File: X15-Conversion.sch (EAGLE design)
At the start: 28 parts, among them U2 LINEAR,AZ1117CR-3.3TRG1DIODES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

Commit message: added files
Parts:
- R7: value 150 -> 600
- R8: value 150 -> 300
- R9: value 150 -> 200
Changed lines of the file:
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@@
 <part name="CONN1" library="CONN, Distribution-Conversion (3)" deviceset="CONVERSION-DISTRIBUTION" device=""/>
 <part name="D4" library="SparkFun-LED" library_urn="urn:adsk.eagle:library:529" deviceset="LED-YELLOW" device="0603" package3d_urn="urn:adsk.eagle:package:39354/1" value="Yellow"/>
-<part name="R7" library="SparkFun-Resistors" library_urn="urn:adsk.eagle:library:532" deviceset="20OHM" device="-0603-1/10W-1%" package3d_urn="urn:adsk.eagle:package:39650/1" value="150"/>
-<part name="R8" library="SparkFun-Resistors" library_urn="urn:adsk.eagle:library:532" deviceset="20OHM" device="-0603-1/10W-1%" package3d_urn="urn:adsk.eagle:package:39650/1" value="150"/>
-<part name="R9" library="SparkFun-Resistors" library_urn="urn:adsk.eagle:library:532" deviceset="20OHM" device="-0603-1/10W-1%" package3d_urn="urn:adsk.eagle:package:39650/1" value="150"/>
+<part name="R7" library="SparkFun-Resistors" library_urn="urn:adsk.eagle:library:532" deviceset="20OHM" device="-0603-1/10W-1%" package3d_urn="urn:adsk.eagle:package:39650/1" value="600"/>
+<part name="R8" library="SparkFun-Resistors" library_urn="urn:adsk.eagle:library:532" deviceset="20OHM" device="-0603-1/10W-1%" package3d_urn="urn:adsk.eagle:package:39650/1" value="300"/>
+<part name="R9" library="SparkFun-Resistors" library_urn="urn:adsk.eagle:library:532" deviceset="20OHM" device="-0603-1/10W-1%" package3d_urn="urn:adsk.eagle:package:39650/1" value="200"/>
 <part name="FRAME3" library="frames" library_urn="urn:adsk.eagle:library:229" deviceset="A4L-LOC" device=""/>
 <part name="D6" library="SparkFun-LED" library_urn="urn:adsk.eagle:library:529" deviceset="LED-RED" device="0603" package3d_urn="urn:adsk.eagle:package:39354/1" value="RED"/>

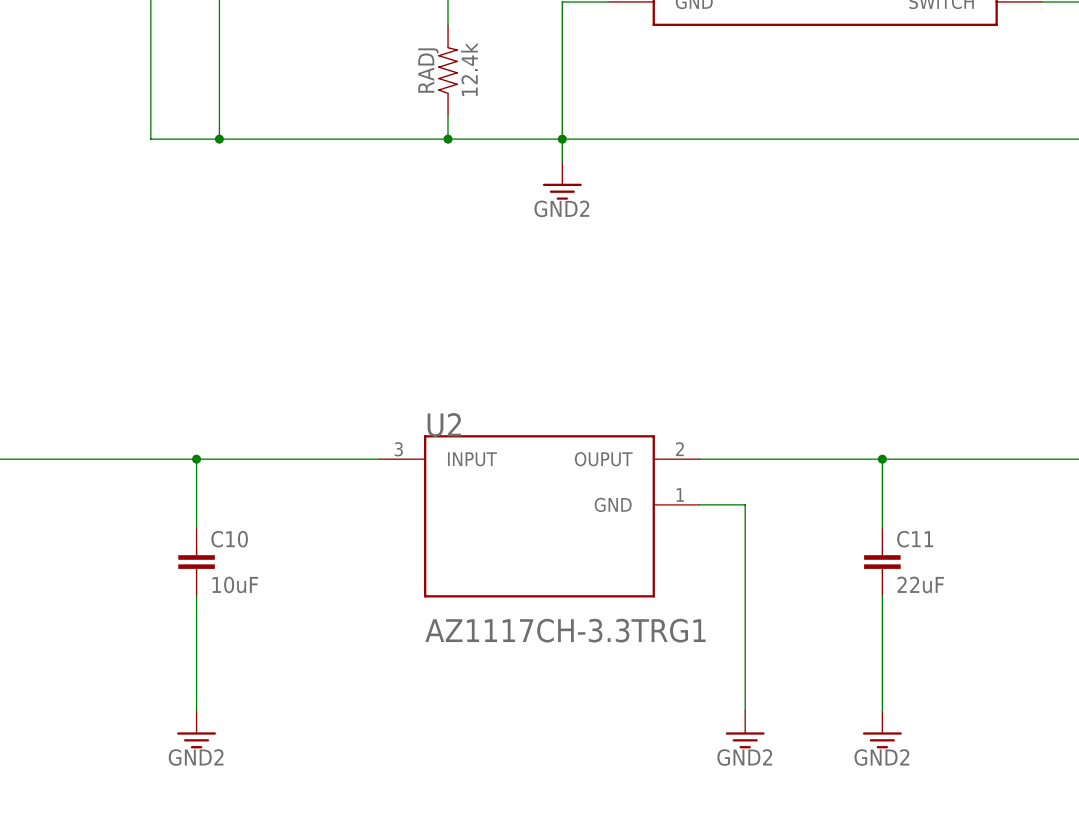
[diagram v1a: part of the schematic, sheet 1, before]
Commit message: Changed the GND
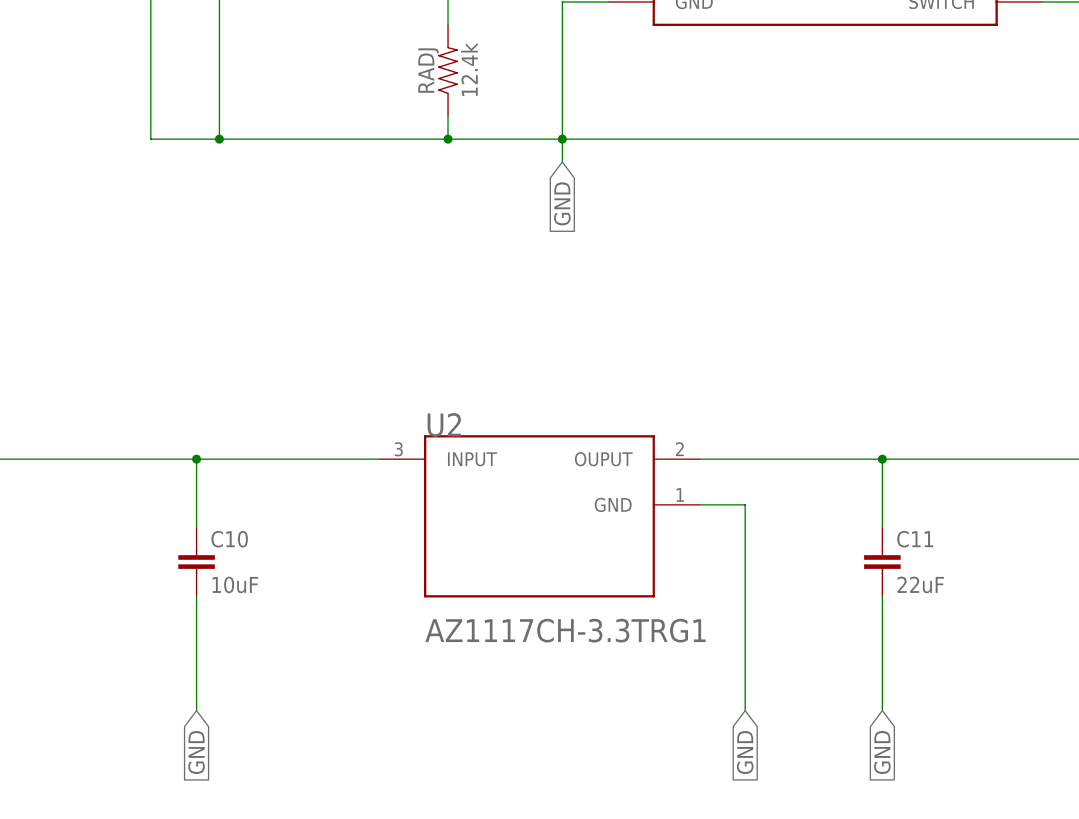
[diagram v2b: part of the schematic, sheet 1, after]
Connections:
- net 3.3V: no longer C10.2, C11.2, CIN1.-, CIN2.2, COUT1.-, COUT2.-, COUT3.-, D2.A, RADJ.1, U$1.GND, U2.GND
- net GND: now also C10.2, C11.2, CIN1.-, CIN2.2, COUT1.-, COUT2.-, COUT3.-, D2.A, RADJ.1, U$1.GND, U2.GND
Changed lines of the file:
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@@
 <part name="CIN1" library="SparkFun-Capacitors" library_urn="urn:adsk.eagle:library:510" deviceset="1000UF" device="-RADIAL-5MM-35V-20%-KIT" package3d_urn="urn:adsk.eagle:package:37421/1" value="180uF"/>
 <part name="RADJ" library="SparkFun-Resistors" library_urn="urn:adsk.eagle:library:532" deviceset="2.0KOHM" device="-0603-1/10W-5%" package3d_urn="urn:adsk.eagle:package:39650/1" value="12.4k"/>
-<part name="GND1" library="SparkFun-PowerSymbols" library_urn="urn:adsk.eagle:library:530" deviceset="GND2" device=""/>
 <part name="D2" library="SparkFun-DiscreteSemi" library_urn="urn:adsk.eagle:library:514" deviceset="DIODE-ZENER" device="-DZ2J150M0L" package3d_urn="urn:adsk.eagle:package:38444/1" value="20V @ 3A"/>
 <part name="CB" library="SparkFun-Capacitors" library_urn="urn:adsk.eagle:library:510" deviceset="4.7PF" device="-0603-50V-5%" package3d_urn="urn:adsk.eagle:package:37414/1" value=".01uF"/>
@@
 <part name="COUT2" library="SparkFun-Capacitors" library_urn="urn:adsk.eagle:library:510" deviceset="1000UF" device="-RADIAL-5MM-35V-20%-KIT" package3d_urn="urn:adsk.eagle:package:37421/1" value="100uF"/>
 <part name="C10" library="SparkFun-Capacitors" library_urn="urn:adsk.eagle:library:510" deviceset="4.7PF" device="-0603-50V-5%" package3d_urn="urn:adsk.eagle:package:37414/1" value="10uF"/>
-<part name="GND2" library="SparkFun-PowerSymbols" library_urn="urn:adsk.eagle:library:530" deviceset="GND2" device=""/>
 <part name="U2" library="X15-Conversion" deviceset="LINEAR,AZ1117CR-3.3TRG1" device="DIODES_AZ1117CH-3.3TRG1_0_0"/>
 <part name="C11" library="SparkFun-Capacitors" library_urn="urn:adsk.eagle:library:510" deviceset="4.7PF" device="-0603-50V-5%" package3d_urn="urn:adsk.eagle:package:37414/1" value="22uF"/>
-<part name="GND3" library="SparkFun-PowerSymbols" library_urn="urn:adsk.eagle:library:530" deviceset="GND2" device=""/>
-<part name="GND4" library="SparkFun-PowerSymbols" library_urn="urn:adsk.eagle:library:530" deviceset="GND2" device=""/>
 <part name="R1" library="SparkFun-Resistors" library_urn="urn:adsk.eagle:library:532" deviceset="2.0KOHM" device="-0603-1/10W-5%" package3d_urn="urn:adsk.eagle:package:39650/1" value="1k"/>
 <part name="R2" library="SparkFun-Resistors" library_urn="urn:adsk.eagle:library:532" deviceset="2.0KOHM" device="-0603-1/10W-5%" package3d_urn="urn:adsk.eagle:package:39650/1" value="3.32k"/>
@@
 <attribute name="VALUE" x="-36.576" y="22.86" size="1.778" layer="96" font="vector" rot="R90" align="top-center"/>
 </instance>
-<instance part="GND1" gate="G$1" x="-25.4" y="10.16" smashed="yes">
-<attribute name="VALUE" x="-25.4" y="8.382" size="1.778" layer="96" align="top-center"/>
-</instance>
 <instance part="D2" gate="G$1" x="40.64" y="25.4" smashed="yes" rot="R90">
 <attribute name="NAME" x="38.608" y="22.86" size="1.778" layer="95" font="vector" rot="R90"/>
@@
 <attribute name="VALUE" x="-64.516" y="-35.179" size="1.778" layer="96" font="vector"/>
 </instance>
-<instance part="GND2" gate="G$1" x="-66.04" y="-50.8" smashed="yes">
-<attribute name="VALUE" x="-66.04" y="-52.578" size="1.778" layer="96" align="top-center"/>
-</instance>
 <instance part="U2" gate="G$0" x="-43.18" y="-12.7" smashed="yes">
 <attribute name="NAME" x="-40.64" y="-15.24" size="2.54" layer="95" align="top-left"/>
@@
 <attribute name="NAME" x="11.684" y="-30.099" size="1.778" layer="95" font="vector"/>
 <attribute name="VALUE" x="11.684" y="-35.179" size="1.778" layer="96" font="vector"/>
-</instance>
-<instance part="GND3" gate="G$1" x="10.16" y="-50.8" smashed="yes">
-<attribute name="VALUE" x="10.16" y="-52.578" size="1.778" layer="96" align="top-center"/>
-</instance>
-<instance part="GND4" gate="G$1" x="-5.08" y="-50.8" smashed="yes">
-<attribute name="VALUE" x="-5.08" y="-52.578" size="1.778" layer="96" align="top-center"/>
 </instance>
 <instance part="R1" gate="G$1" x="53.34" y="58.42" smashed="yes">
@@
 <wire x1="58.42" y1="58.42" x2="81.28" y2="58.42" width="0.1524" layer="91"/>
 <label x="81.28" y="58.42" size="1.778" layer="95" xref="yes"/>
+</segment>
+<segment>
+<wire x1="-63.5" y1="15.24" x2="-71.12" y2="15.24" width="0.1524" layer="91"/>
+<pinref part="CIN1" gate="G$1" pin="-"/>
+<wire x1="-71.12" y1="33.02" x2="-71.12" y2="15.24" width="0.1524" layer="91"/>
+<pinref part="CIN2" gate="G$1" pin="2"/>
+<wire x1="-63.5" y1="33.02" x2="-63.5" y2="15.24" width="0.1524" layer="91"/>
+<junction x="-63.5" y="15.24"/>
+<pinref part="RADJ" gate="G$1" pin="1"/>
+<wire x1="-38.1" y1="17.78" x2="-38.1" y2="15.24" width="0.1524" layer="91"/>
+<wire x1="-38.1" y1="15.24" x2="-63.5" y2="15.24" width="0.1524" layer="91"/>
+<pinref part="U$1" gate="G$1" pin="GND"/>
+<wire x1="-20.32" y1="30.48" x2="-25.4" y2="30.48" width="0.1524" layer="91"/>
+<wire x1="-25.4" y1="30.48" x2="-25.4" y2="15.24" width="0.1524" layer="91"/>
+<wire x1="-25.4" y1="15.24" x2="-38.1" y2="15.24" width="0.1524" layer="91"/>
+<junction x="-38.1" y="15.24"/>
+<wire x1="-25.4" y1="15.24" x2="-25.4" y2="12.7" width="0.1524" layer="91"/>
+<junction x="-25.4" y="15.24"/>
+<wire x1="-25.4" y1="15.24" x2="40.64" y2="15.24" width="0.1524" layer="91"/>
+<pinref part="D2" gate="G$1" pin="A"/>
+<wire x1="40.64" y1="15.24" x2="40.64" y2="22.86" width="0.1524" layer="91"/>
+<pinref part="COUT1" gate="G$1" pin="-"/>
+<wire x1="60.96" y1="20.32" x2="60.96" y2="15.24" width="0.1524" layer="91"/>
+<wire x1="60.96" y1="15.24" x2="40.64" y2="15.24" width="0.1524" layer="91"/>
+<junction x="40.64" y="15.24"/>
+<pinref part="COUT2" gate="G$1" pin="-"/>
+<wire x1="71.12" y1="20.32" x2="71.12" y2="15.24" width="0.1524" layer="91"/>
+<wire x1="71.12" y1="15.24" x2="60.96" y2="15.24" width="0.1524" layer="91"/>
+<junction x="60.96" y="15.24"/>
+<pinref part="COUT3" gate="G$1" pin="-"/>
+<wire x1="78.74" y1="20.32" x2="78.74" y2="15.24" width="0.1524" layer="91"/>
+<wire x1="78.74" y1="15.24" x2="71.12" y2="15.24" width="0.1524" layer="91"/>
+<junction x="71.12" y="15.24"/>
+<label x="-25.4" y="12.7" size="1.778" layer="95" rot="R270" xref="yes"/>
+</segment>
+<segment>
+<pinref part="C10" gate="G$1" pin="2"/>
+<wire x1="-66.04" y1="-35.56" x2="-66.04" y2="-48.26" width="0.1524" layer="91"/>
+<label x="-66.04" y="-48.26" size="1.778" layer="95" rot="R270" xref="yes"/>
+</segment>
+<segment>
+<pinref part="U2" gate="G$0" pin="GND"/>
+<wire x1="-10.16" y1="-25.4" x2="-5.08" y2="-25.4" width="0.1524" layer="91"/>
+<wire x1="-5.08" y1="-25.4" x2="-5.08" y2="-48.26" width="0.1524" layer="91"/>
+<label x="-5.08" y="-48.26" size="1.778" layer="95" rot="R270" xref="yes"/>
+</segment>
+<segment>
+<pinref part="C11" gate="G$1" pin="2"/>
+<wire x1="10.16" y1="-35.56" x2="10.16" y2="-48.26" width="0.1524" layer="91"/>
+<label x="10.16" y="-48.26" size="1.778" layer="95" rot="R270" xref="yes"/>
 </segment>
 </net>
@@
 <net name="3.3V" class="0">
 <segment>
-<wire x1="-63.5" y1="15.24" x2="-71.12" y2="15.24" width="0.1524" layer="91"/>
-<pinref part="CIN1" gate="G$1" pin="-"/>
-<wire x1="-71.12" y1="33.02" x2="-71.12" y2="15.24" width="0.1524" layer="91"/>
-<pinref part="CIN2" gate="G$1" pin="2"/>
-<wire x1="-63.5" y1="33.02" x2="-63.5" y2="15.24" width="0.1524" layer="91"/>
-<junction x="-63.5" y="15.24"/>
-<pinref part="RADJ" gate="G$1" pin="1"/>
-<wire x1="-38.1" y1="17.78" x2="-38.1" y2="15.24" width="0.1524" layer="91"/>
-<wire x1="-38.1" y1="15.24" x2="-63.5" y2="15.24" width="0.1524" layer="91"/>
-<pinref part="U$1" gate="G$1" pin="GND"/>
-<wire x1="-20.32" y1="30.48" x2="-25.4" y2="30.48" width="0.1524" layer="91"/>
-<wire x1="-25.4" y1="30.48" x2="-25.4" y2="15.24" width="0.1524" layer="91"/>
-<wire x1="-25.4" y1="15.24" x2="-38.1" y2="15.24" width="0.1524" layer="91"/>
-<junction x="-38.1" y="15.24"/>
-<wire x1="-25.4" y1="15.24" x2="-25.4" y2="12.7" width="0.1524" layer="91"/>
-<junction x="-25.4" y="15.24"/>
-<pinref part="GND1" gate="G$1" pin="3.3V"/>
-<wire x1="-25.4" y1="15.24" x2="40.64" y2="15.24" width="0.1524" layer="91"/>
-<pinref part="D2" gate="G$1" pin="A"/>
-<wire x1="40.64" y1="15.24" x2="40.64" y2="22.86" width="0.1524" layer="91"/>
-<pinref part="COUT1" gate="G$1" pin="-"/>
-<wire x1="60.96" y1="20.32" x2="60.96" y2="15.24" width="0.1524" layer="91"/>
-<wire x1="60.96" y1="15.24" x2="40.64" y2="15.24" width="0.1524" layer="91"/>
-<junction x="40.64" y="15.24"/>
-<pinref part="COUT2" gate="G$1" pin="-"/>
-<wire x1="71.12" y1="20.32" x2="71.12" y2="15.24" width="0.1524" layer="91"/>
-<wire x1="71.12" y1="15.24" x2="60.96" y2="15.24" width="0.1524" layer="91"/>
-<junction x="60.96" y="15.24"/>
-<pinref part="COUT3" gate="G$1" pin="-"/>
-<wire x1="78.74" y1="20.32" x2="78.74" y2="15.24" width="0.1524" layer="91"/>
-<wire x1="78.74" y1="15.24" x2="71.12" y2="15.24" width="0.1524" layer="91"/>
-<junction x="71.12" y="15.24"/>
-</segment>
-<segment>
-<pinref part="C10" gate="G$1" pin="2"/>
-<wire x1="-66.04" y1="-35.56" x2="-66.04" y2="-48.26" width="0.1524" layer="91"/>
-<pinref part="GND2" gate="G$1" pin="3.3V"/>
-</segment>
-<segment>
-<pinref part="C11" gate="G$1" pin="2"/>
-<wire x1="10.16" y1="-35.56" x2="10.16" y2="-48.26" width="0.1524" layer="91"/>
-<pinref part="GND3" gate="G$1" pin="3.3V"/>
-</segment>
-<segment>
 <pinref part="U2" gate="G$0" pin="OUPUT"/>
 <wire x1="-10.16" y1="-20.32" x2="10.16" y2="-20.32" width="0.1524" layer="91"/>
@@
 <label x="38.1" y="-20.32" size="1.778" layer="95" xref="yes"/>
 </segment>
-<segment>
-<pinref part="U2" gate="G$0" pin="GND"/>
-<wire x1="-10.16" y1="-25.4" x2="-5.08" y2="-25.4" width="0.1524" layer="91"/>
-<wire x1="-5.08" y1="-25.4" x2="-5.08" y2="-48.26" width="0.1524" layer="91"/>
-<pinref part="GND4" gate="G$1" pin="3.3V"/>
-</segment>
-</net>
+</net>

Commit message: Changed the diode
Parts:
- D2: device SparkFun-DiscreteSemi:DIODE-ZENER-DZ2J150M0L -> SparkFun-DiscreteSemi:DIODE-ZENER-MMSZ5232BS
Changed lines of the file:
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@@
 <part name="CIN1" library="SparkFun-Capacitors" library_urn="urn:adsk.eagle:library:510" deviceset="1000UF" device="-RADIAL-5MM-35V-20%-KIT" package3d_urn="urn:adsk.eagle:package:37421/1" value="180uF"/>
 <part name="RADJ" library="SparkFun-Resistors" library_urn="urn:adsk.eagle:library:532" deviceset="2.0KOHM" device="-0603-1/10W-5%" package3d_urn="urn:adsk.eagle:package:39650/1" value="12.4k"/>
-<part name="D2" library="SparkFun-DiscreteSemi" library_urn="urn:adsk.eagle:library:514" deviceset="DIODE-ZENER" device="-DZ2J150M0L" package3d_urn="urn:adsk.eagle:package:38444/1" value="20V @ 3A"/>
+<part name="D2" library="SparkFun-DiscreteSemi" library_urn="urn:adsk.eagle:library:514" deviceset="DIODE-ZENER" device="-MMSZ5232BS" package3d_urn="urn:adsk.eagle:package:38441/1" value="20V @ 3A"/>
 <part name="CB" library="SparkFun-Capacitors" library_urn="urn:adsk.eagle:library:510" deviceset="4.7PF" device="-0603-50V-5%" package3d_urn="urn:adsk.eagle:package:37414/1" value=".01uF"/>
 <part name="L1" library="ngspice-simulation" library_urn="urn:adsk.eagle:library:527439" deviceset="L" device="" value="22uH"/>
